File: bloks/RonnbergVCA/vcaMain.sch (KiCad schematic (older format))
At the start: 21 parts, among them U1 TL074, U2 CA3080

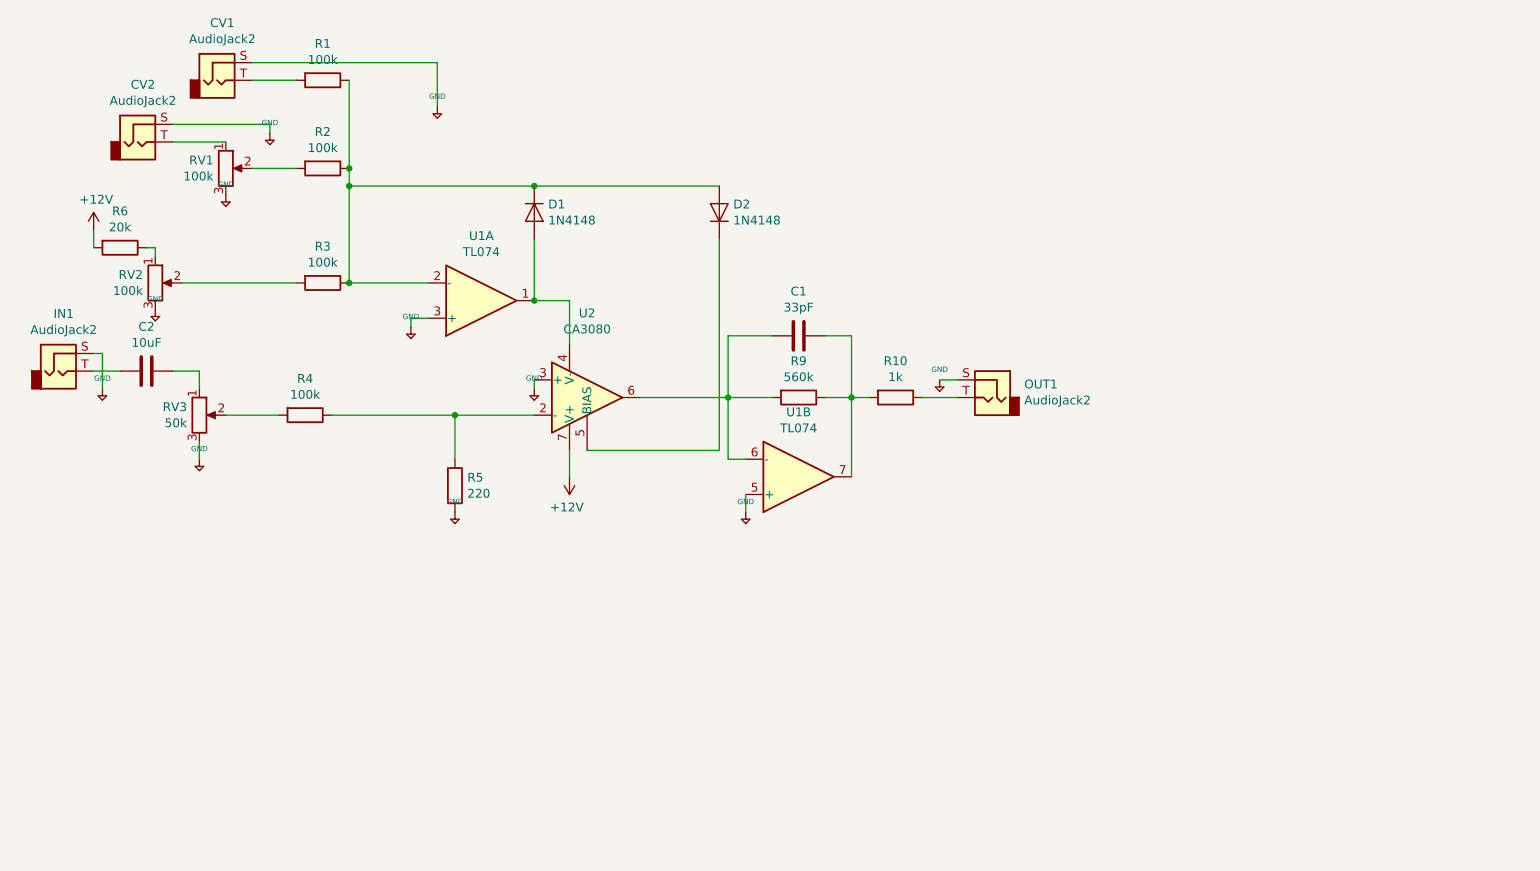
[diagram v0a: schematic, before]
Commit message: Split Ronnberg VCA into seperate projects for control and main
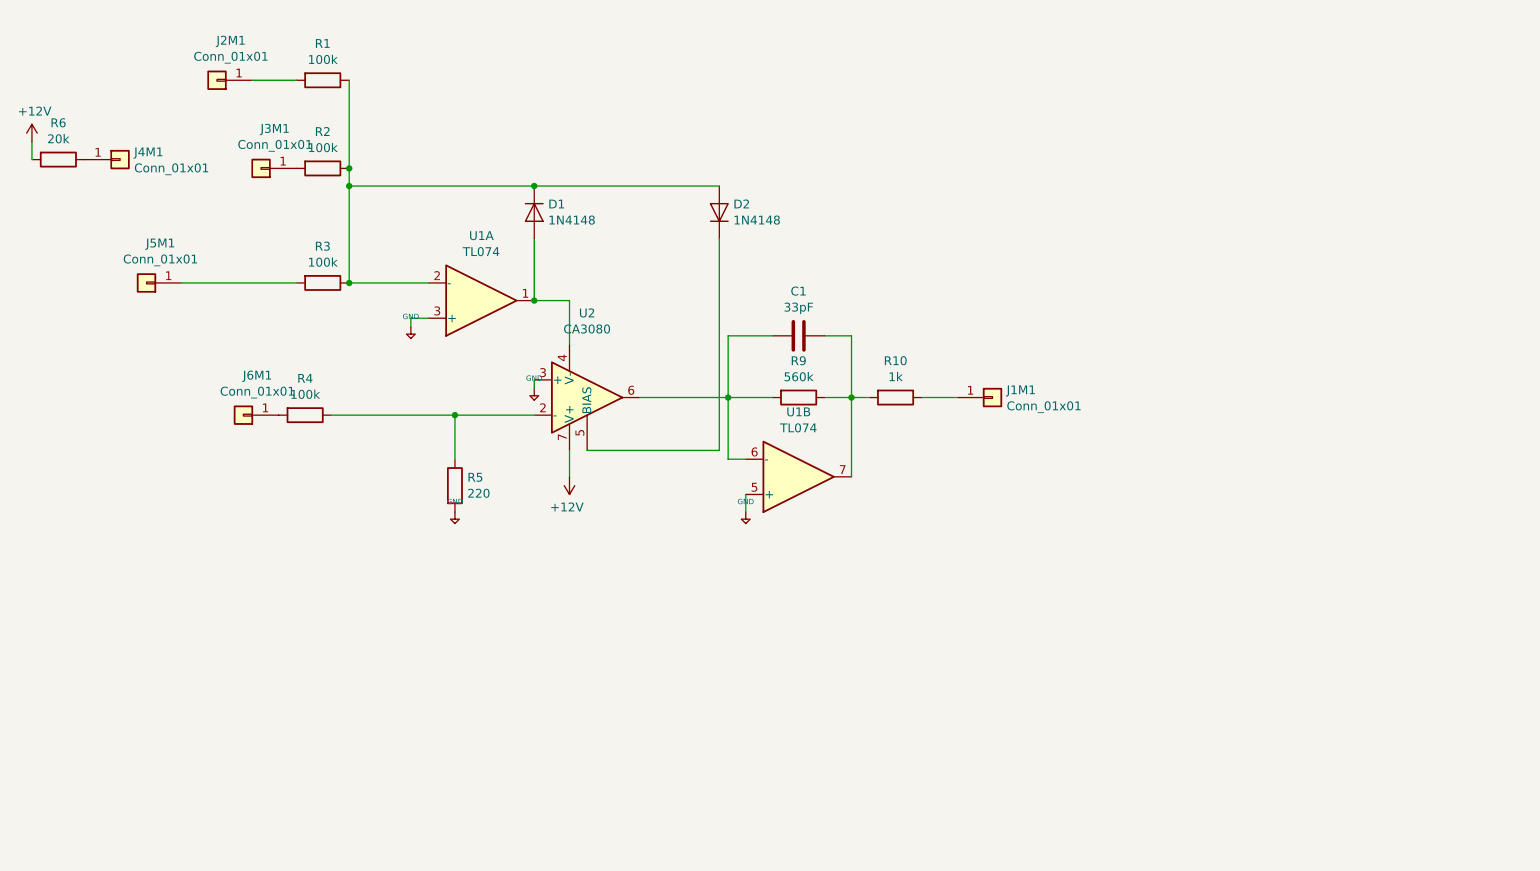
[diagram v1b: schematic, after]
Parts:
- removed C2: 10uF, Capacitor_THT:C_Disc_D4.3mm_W1.9mm_P5.00mm, symbol Device:C
- removed CV1, CV2, IN1, OUT1: AudioJack2, Connector_Audio-2:Jack_3.5mm_QingPu_WQP-PJ398SM_Vertical_CircularHoles, symbol Connector:AudioJack2
- removed RV1, RV2: 100k, MyModules:RV16A-41-JRL, symbol Device:R_POT
- removed RV3: 50k, MyModules:RV16A-41-JRL, symbol Device:R_POT
- added J1M1, J2M1, J3M1, J4M1, J5M1, J6M1: Conn_01x01, Connector_PinSocket_2.54mm:PinSocket_1x01_P2.54mm_Vertical, symbol Connector_Generic:Conn_01x01
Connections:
- net at R2.2: now also J3M1.1 (Pin_1)
- net at R6.1: now also J4M1.1 (Pin_1)
- net at R3.2: now also J5M1.1 (Pin_1)
- net at R1.2: now also J2M1.1 (Pin_1)
- net at R4.2: now also J6M1.1 (Pin_1)
- net at R10.1: now also J1M1.1 (Pin_1)
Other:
- moved on the sheet: R6

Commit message: pcb layout
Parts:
- removed U1: TL074, Package_DIP:DIP-14_W7.62mm, symbol Amplifier_Operational:TL074
- added J1, J2, J3, J4, J5, J6: Conn_02x03_Odd_Even, Connector_PinHeader_2.54mm:PinHeader_2x03_P2.54mm_Horizontal, symbol Connector_Generic:Conn_02x03_Odd_Even
- added J10, J11, J12, J7, J8, J9: Conn_02x03_Odd_Even, Connector_PinSocket_2.54mm:PinSocket_2x03_P2.54mm_Horizontal, symbol Connector_Generic:Conn_02x03_Odd_Even
- added J7M1: Conn_01x01, Connector_PinSocket_2.54mm:PinSocket_1x01_P2.54mm_Vertical, symbol Connector_Generic:Conn_01x01
- added U1: TL072, Package_DIP:DIP-8_W7.62mm, symbol Amplifier_Operational:TL072
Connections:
- net +12V: now also J1.5 (Pin_5), J1.6 (Pin_6), J10.5 (Pin_5), J10.6 (Pin_6), J11.5 (Pin_5), J11.6 (Pin_6), J12.5 (Pin_5), J12.6 (Pin_6), J2.5 (Pin_5), J2.6 (Pin_6), J3.5 (Pin_5), J3.6 (Pin_6), J4.5 (Pin_5), J4.6 (Pin_6), J5.5 (Pin_5), J5.6 (Pin_6), J6.5 (Pin_5), J6.6 (Pin_6), J7.5 (Pin_5), J7.6 (Pin_6), J8.5 (Pin_5), J8.6 (Pin_6), J9.5 (Pin_5), J9.6 (Pin_6), U1.8 (V+)
- net +5V: now also J1.1 (Pin_1), J1.2 (Pin_2), J10.1 (Pin_1), J10.2 (Pin_2), J11.1 (Pin_1), J11.2 (Pin_2), J12.1 (Pin_1), J12.2 (Pin_2), J2.1 (Pin_1), J2.2 (Pin_2), J3.1 (Pin_1), J3.2 (Pin_2), J4.1 (Pin_1), J4.2 (Pin_2), J5.1 (Pin_1), J5.2 (Pin_2), J6.1 (Pin_1), J6.2 (Pin_2), J7.1 (Pin_1), J7.2 (Pin_2), J8.1 (Pin_1), J8.2 (Pin_2), J9.1 (Pin_1), J9.2 (Pin_2); no longer R5.2, U2.3 (+)
- net at D1.1 (K), D2.2 (A), R1.1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: now also U1.3 (+)
- net at D1.2 (A), U2.4 (V-): now also U1.1
- net at C1.2, R9.2, U2.6: now also U1.5 (+)
- net at C1.1, R10.2, R9.1: now also U1.7
- new net GND: J1.3 (Pin_3), J1.4 (Pin_4), J10.3 (Pin_3), J10.4 (Pin_4), J11.3 (Pin_3), J11.4 (Pin_4), J12.3 (Pin_3), J12.4 (Pin_4), J2.3 (Pin_3), J2.4 (Pin_4), J3.3 (Pin_3), J3.4 (Pin_4), J4.3 (Pin_3), J4.4 (Pin_4), J5.3 (Pin_3), J5.4 (Pin_4), J6.3 (Pin_3), J6.4 (Pin_4), J7.3 (Pin_3), J7.4 (Pin_4), J7M1.1 (Pin_1), J8.3 (Pin_3), J8.4 (Pin_4), J9.3 (Pin_3), J9.4 (Pin_4), R5.2, U1.2 (-), U1.4 (V-), U1.6 (-), U2.3 (+)
